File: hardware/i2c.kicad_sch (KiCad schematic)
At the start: 0 parts

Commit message: block refactoring
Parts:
- added C7: 1uF, Capacitor_SMD:C_0603_1608Metric, symbol Device:C
- added D16: RCLAMP0502B, Package_TO_SOT_SMD:SOT-416, symbol Power_Protection:RCLAMP0502B
- added D17: D_TVS_3V3, Diode_SMD:D_SOD-123, symbol Device:D_TVS
- added J5 (x2): Conn_01x04/QWiiC, Connector_JST:JST_PH_B4B-PH-K_1x04_P2.00mm_Vertical, symbol Connector_Generic:Conn_01x04
- added R7, R8: 2.7k, Resistor_SMD:R_0603_1608Metric, symbol Device:R
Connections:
- new net I2C_3V3: C7.1, D17.2 (A2), J5.2 (Pin_2), J5.2 (Pin_2), R7.1, R8.1
- new net I2C_GND: C7.2, D16.3 (A), D17.1 (A1), J5.1 (Pin_1), J5.1 (Pin_1)
- new net I2C_SCL: D16.2 (K2), J5.4 (Pin_4), J5.4 (Pin_4), R7.2
- new net I2C_SDA: D16.1 (K1), J5.3 (Pin_3), J5.3 (Pin_3), R8.2
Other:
- note added: "+3.3V"
- note added: "GND"
- note added: "I2C (qwiic) x 2"
- note added: "SCL"
- note added: "SDA"

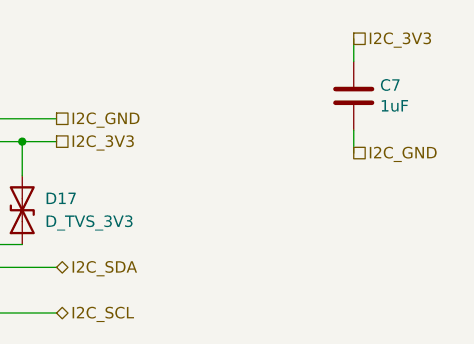
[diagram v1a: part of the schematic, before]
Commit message: Added 3D models and ran freerouting
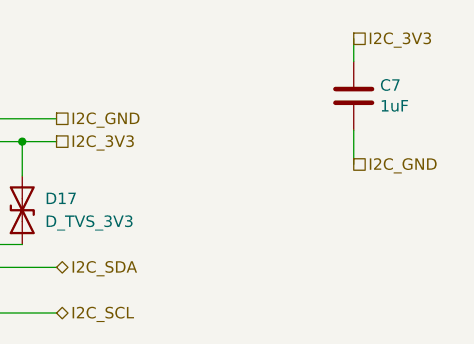
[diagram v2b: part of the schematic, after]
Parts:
- C7: footprint Capacitor_SMD:C_0603_1608Metric -> Capacitor_SMD:C_0805_2012Metric
- R7, R8: footprint Resistor_SMD:R_0603_1608Metric -> Resistor_SMD:R_0805_2012Metric
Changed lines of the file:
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@@
     (stroke (width 0) (type default))
   )
-  (wire (pts (xy 177.8 78.74) (xy 177.8 76.2))
+  (wire (pts (xy 177.8 80.01) (xy 177.8 76.2))
     (stroke (width 0) (type default))
   )
@@
     (effects (font (size 1.27 1.27)) (justify left))
   )
-  (hierarchical_label "I2C_GND" (shape passive) (at 177.8 78.74 0) (fields_autoplaced)
+  (hierarchical_label "I2C_GND" (shape passive) (at 177.8 80.01 0) (fields_autoplaced)
     (effects (font (size 1.27 1.27)) (justify left))
   )
@@
       (effects (font (size 1.27 1.27)))
     )
-    (property "Footprint" "Resistor_SMD:R_0603_1608Metric" (at 113.538 83.82 90)
+    (property "Footprint" "Resistor_SMD:R_0805_2012Metric" (at 113.538 83.82 90)
       (effects (font (size 1.27 1.27)) hide)
     )
@@
       (effects (font (size 1.27 1.27)))
     )
-    (property "Footprint" "Resistor_SMD:R_0603_1608Metric" (at 104.648 83.82 90)
+    (property "Footprint" "Resistor_SMD:R_0805_2012Metric" (at 104.648 83.82 90)
       (effects (font (size 1.27 1.27)) hide)
     )
@@
       (effects (font (size 1.27 1.27)) (justify left))
     )
-    (property "Footprint" "Capacitor_SMD:C_0603_1608Metric" (at 178.7652 76.2 0)
+    (property "Footprint" "Capacitor_SMD:C_0805_2012Metric" (at 178.7652 76.2 0)
       (effects (font (size 1.27 1.27)) hide)
     )
